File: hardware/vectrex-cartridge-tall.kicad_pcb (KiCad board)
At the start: 2 copper layers, 48 x 66.1 mm, 18 parts, among them CON1 vectrex-edge-connector, SW1 SW_DIP_x03, U1 AT27C256R-70PU / AT27C512R-70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, U2 DS2431+ TO-92

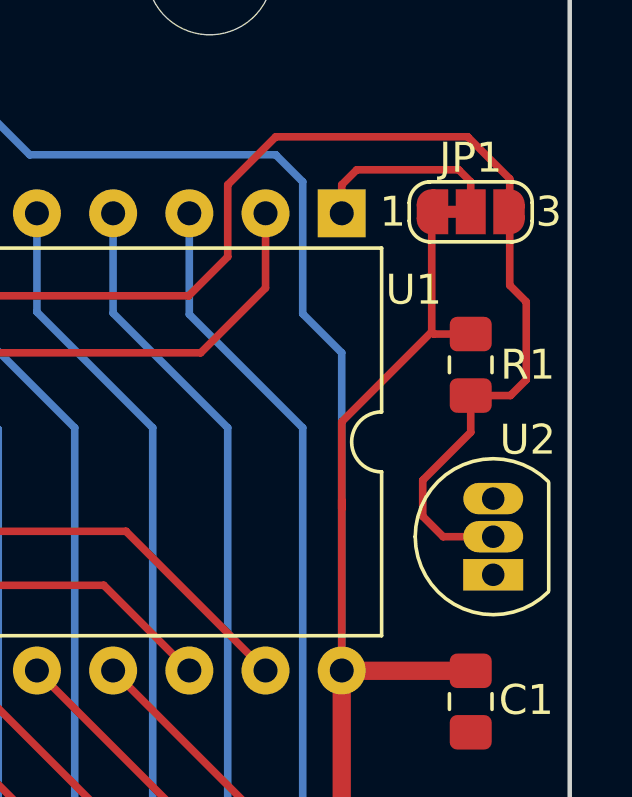
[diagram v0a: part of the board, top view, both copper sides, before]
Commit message: migrate 3D shapes to built-in KiCad 6.x location
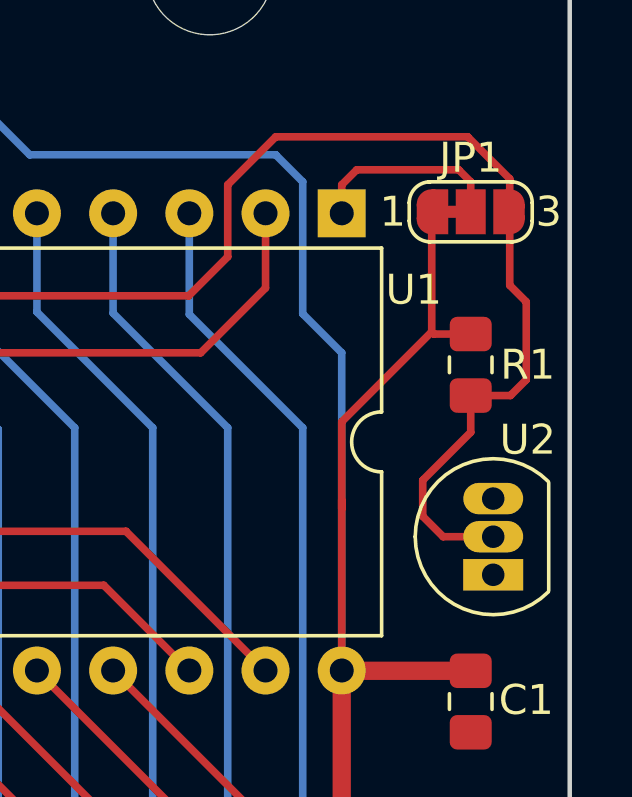
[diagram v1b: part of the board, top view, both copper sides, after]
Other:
- net class Default removed
- net class Large removed
